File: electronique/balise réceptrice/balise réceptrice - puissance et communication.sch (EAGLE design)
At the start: 27 parts, among them IC1 786TV

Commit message: release modele 3D + elec :D
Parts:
- added LED1, LED2, LED3, LED4: (no value), led:LED3MM
- added R13: 22K, resistor:R-EU_0204/7
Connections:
- new net N$23: LED1.A, U$2.6
- new net N$24: LED2.A, U$2.5
- new net N$25: LED3.A, U$2.4
- new net N$26: LED4.A, U$2.3
- new net N$27: LED1.C, LED2.C, LED3.C, LED4.C, R13.1
- net GND: now also R13.2
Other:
- moved on the sheet: C1, DC1, IC1, JP1, SUPPLY, XB1

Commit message: ajout des fichiers gerber et excellon
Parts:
- added U$3: 1RT, switch:1RT
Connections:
- new net N$28: SUPPLY.2, U$3.P
- net N$22: now also U$3.S; no longer SUPPLY.2
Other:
- moved on the sheet: SUPPLY
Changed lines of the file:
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@@
 <part name="LED4" library="led" deviceset="LED" device="3MM"/>
 <part name="SUPPLY18" library="supply2" deviceset="GND" device=""/>
+<part name="U$3" library="switch" deviceset="1RT" device=""/>
 </parts>
 <sheets>
@@
 <instances>
 <instance part="U$1" gate="G$1" x="71.12" y="33.02"/>
-<instance part="SUPPLY" gate="G$1" x="0" y="38.1" rot="R180"/>
+<instance part="SUPPLY" gate="G$1" x="-15.24" y="38.1" rot="R180"/>
 <instance part="JP2" gate="A" x="78.74" y="73.66" rot="R180"/>
 <instance part="SUPPLY1" gate="+15V" x="91.44" y="43.18"/>
@@
 <instance part="LED4" gate="G$1" x="180.34" y="10.16" rot="R90"/>
 <instance part="SUPPLY18" gate="GND" x="187.96" y="-7.62"/>
+<instance part="U$3" gate="G$1" x="5.08" y="43.18" rot="R270"/>
 </instances>
 <busses>
@@
 <wire x1="27.94" y1="27.94" x2="27.94" y2="30.48" width="0.1524" layer="91"/>
 <pinref part="SUPPLY" gate="G$1" pin="1"/>
-<wire x1="2.54" y1="35.56" x2="12.7" y2="35.56" width="0.1524" layer="91"/>
+<wire x1="-12.7" y1="35.56" x2="12.7" y2="35.56" width="0.1524" layer="91"/>
 <wire x1="12.7" y1="35.56" x2="12.7" y2="27.94" width="0.1524" layer="91"/>
 <wire x1="12.7" y1="27.94" x2="27.94" y2="27.94" width="0.1524" layer="91"/>
@@
 <pinref part="JP1" gate="A" pin="2"/>
 <wire x1="27.94" y1="27.94" x2="27.94" y2="20.32" width="0.1524" layer="91"/>
-</segment>
-</net>
-<net name="N$22" class="0">
-<segment>
-<pinref part="SUPPLY" gate="G$1" pin="2"/>
-<pinref part="DC1" gate="G$1" pin="VIN"/>
-<wire x1="2.54" y1="38.1" x2="15.24" y2="38.1" width="0.1524" layer="91"/>
 </segment>
 </net>
@@
 </segment>
 </net>
+<net name="N$22" class="0">
+<segment>
+<pinref part="DC1" gate="G$1" pin="VIN"/>
+<pinref part="U$3" gate="G$1" pin="S"/>
+<wire x1="10.16" y1="38.1" x2="15.24" y2="38.1" width="0.1524" layer="91"/>
+</segment>
+</net>
+<net name="N$28" class="0">
+<segment>
+<pinref part="SUPPLY" gate="G$1" pin="2"/>
+<wire x1="-12.7" y1="38.1" x2="-5.08" y2="38.1" width="0.1524" layer="91"/>
+<wire x1="-5.08" y1="38.1" x2="-5.08" y2="40.64" width="0.1524" layer="91"/>
+<pinref part="U$3" gate="G$1" pin="P"/>
+<wire x1="-5.08" y1="40.64" x2="0" y2="40.64" width="0.1524" layer="91"/>
+</segment>
+</net>

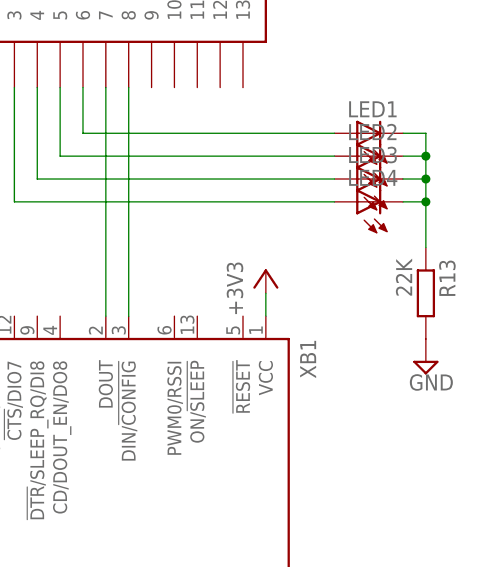
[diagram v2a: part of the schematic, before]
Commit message: Ajout doc + mise a jour des modeles 3D
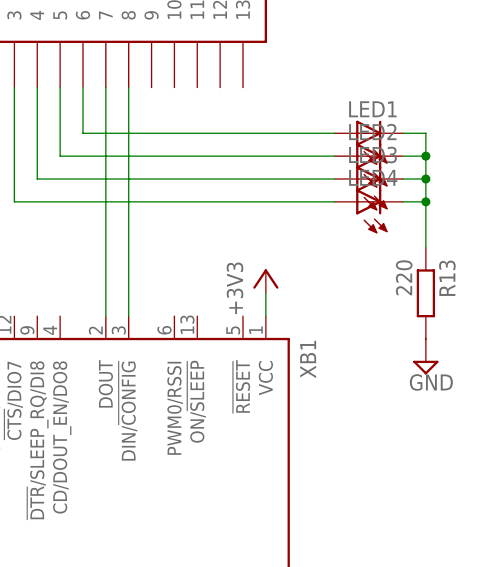
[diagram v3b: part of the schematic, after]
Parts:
- R13: value 22K -> 220
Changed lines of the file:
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@@
 <part name="JP1" library="jumper" deviceset="JP1E" device=""/>
 <part name="SUPPLY17" library="supply2" deviceset="GND" device=""/>
-<part name="R13" library="resistor" deviceset="R-EU_" device="0204/7" value="22K"/>
+<part name="R13" library="resistor" deviceset="R-EU_" device="0204/7" value="220"/>
 <part name="LED1" library="led" deviceset="LED" device="3MM"/>
 <part name="LED2" library="led" deviceset="LED" device="3MM"/>
